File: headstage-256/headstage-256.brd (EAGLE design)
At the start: 32 x 32 mm, 302 parts, among them J2 MMCX-J-P-H-ST-SM1/U.FL-R-SMT(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, J4 PINHD-2X5+4DF40-HEAD, J5 5041940270, U1 OPA170, U10 NRF24L01QFN, U11 CAT4016_QFN, U12 CAT4016_QFN, U13 TPL0501_UQFN, U14 TPL0501_UQFN, U15 MICROSD_473093751, U16 10M08SAM15317G, U17 Si8487DB, U18 MAX17048_WLP, U19 BNO055, U2 OPA170, U20 TPS61202, U21 RHD2064_BGA, U22 RHD2064_BGA, U23 TS4231, U24 TS4231, U25 LT3463, U26 ASCO-50.000MHZ-EK-T3, U27 TS4231, U28 TLV70733, U29 TS4231, U3 INA826, U30 RHD2064_BGA, U31 RHD2064_BGA, U32 MIC23150, U33 TS4231, U34 TS4231, U35 TPS8268180, U4 INA826, U5 DAC5311, U6 DAC5311, U7 DS90UB913A_WQFN, U8 DG509B, U9 DG509B, Y1 FW1600008, Y2 ECS-.327-12.5-1210-TR

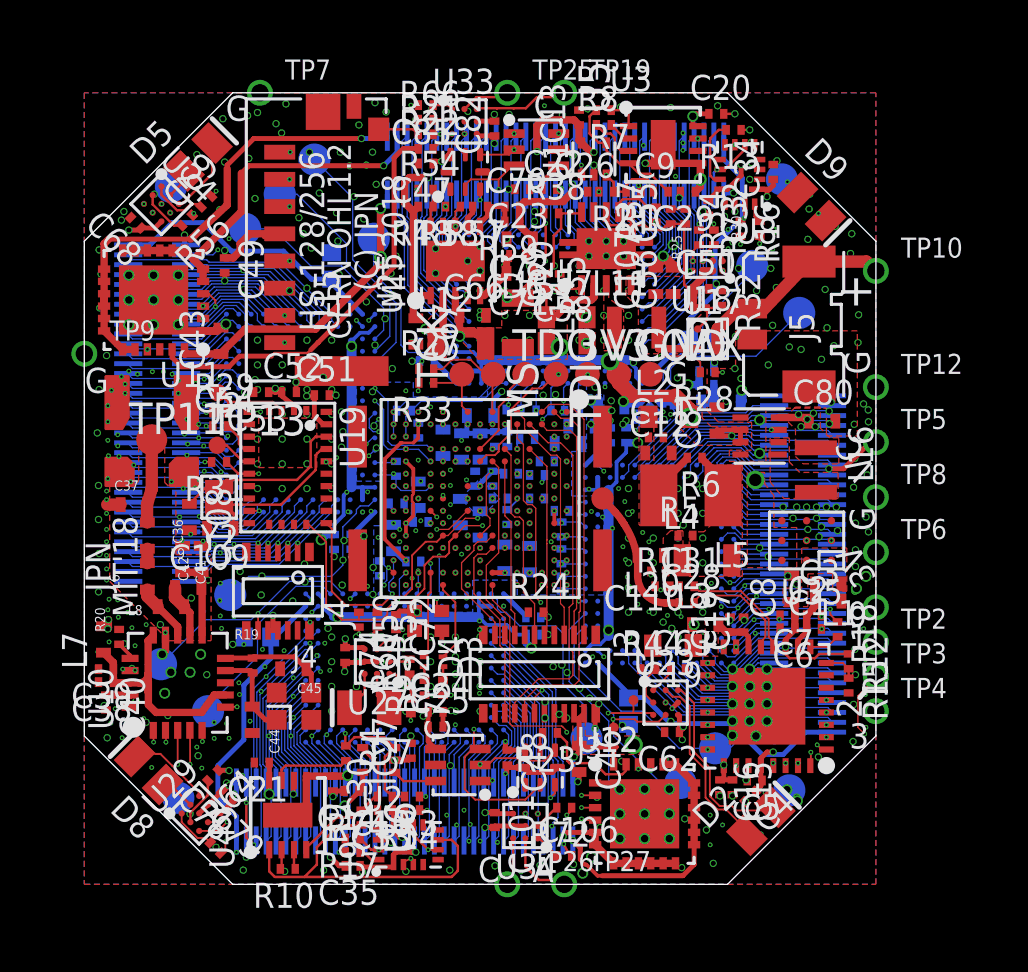
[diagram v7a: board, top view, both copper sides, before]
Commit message: Even more catious routing on headstage-256
- Serializer digital lines completely avoid bias-t network's inductor
and pads.
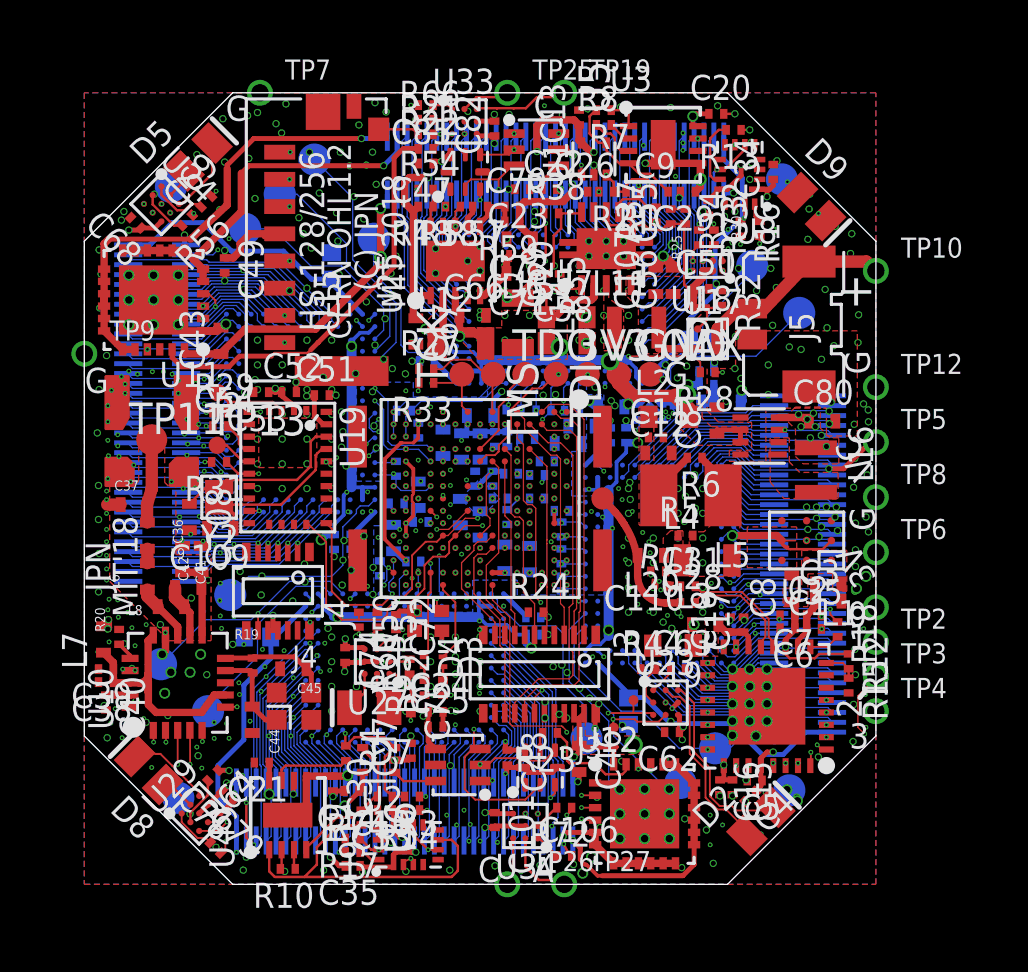
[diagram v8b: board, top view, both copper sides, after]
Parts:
- moved R11 0.05 mm to (7.37, -3.90), turned to 352 degrees
- moved C28 0.05 mm to (8.40, -4.62)
- moved C31 0.05 mm to (8.40, -3.95)
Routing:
- net VCOAX: track 70.4 -> 77.9 mm, vias 16 -> 12
- net HSYNC: track 18.4 -> 21.7 mm
- net DIN8: track 18.2 -> 21.5 mm
- net DIN9: track 17.9 -> 21.2 mm
- net DIN10: track 19.3 -> 22.5 mm
- net SERDES_EN: track 14.8 -> 17.9 mm
- net DIN11: track 19.5 -> 22.6 mm
- net SERDES_SDA: track 17.9 -> 20.8 mm
- net SERDES_SCL: track 18.5 -> 21.4 mm
- net PCLK: track 22.0 -> 24.8 mm
- net VSYNC: track 20.0 -> 22.8 mm
- net GND: track 40.4 -> 39.5 mm, vias 451 -> 455
- net LIPO_QSTRT: track 10.9 -> 10.2 mm
- net !LIPO_ALRT: track 14.3 -> 13.7 mm
- net +3V3: vias 50 -> 53
